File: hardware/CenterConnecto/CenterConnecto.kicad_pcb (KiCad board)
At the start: 2 copper layers, 21.5 x 12 mm, 4 parts, among them J1 Conn_01x10, J2 Conn_01x10

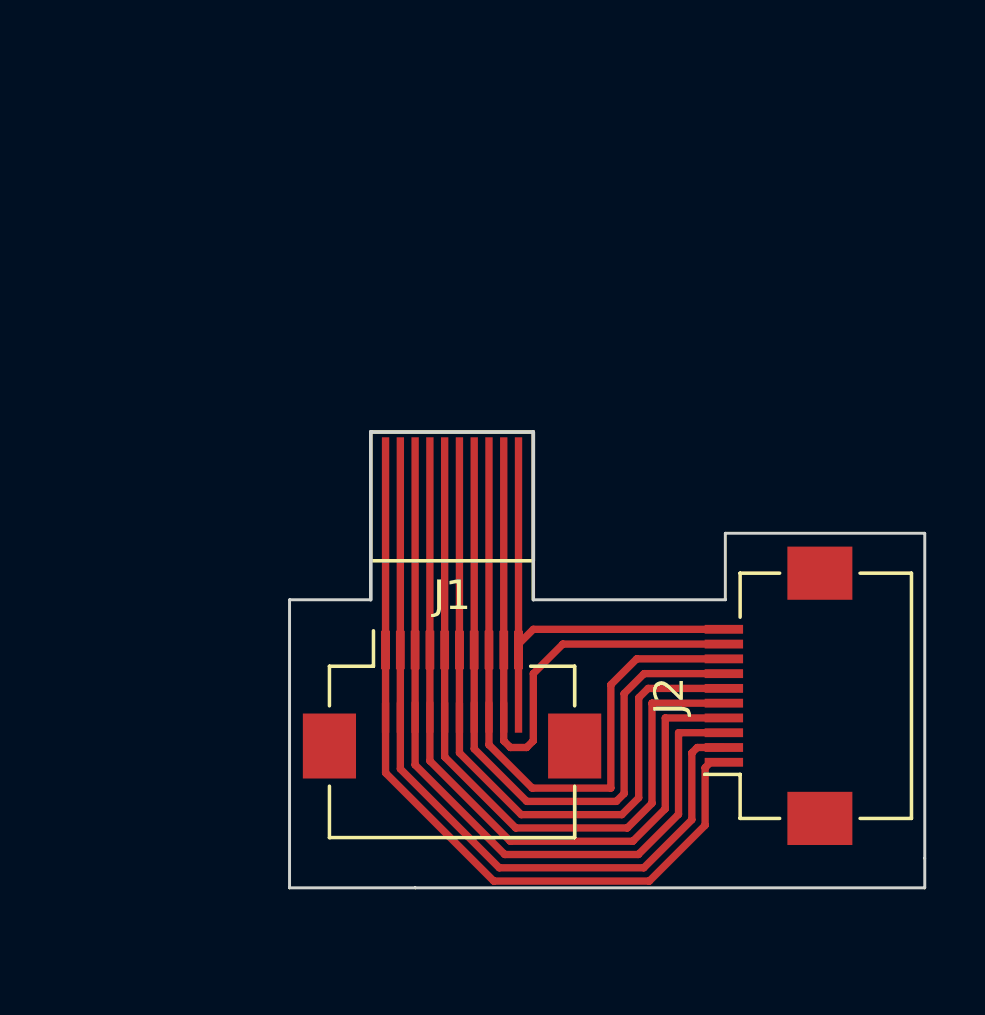
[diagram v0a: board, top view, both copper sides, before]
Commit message: Added initial left buttons fpc
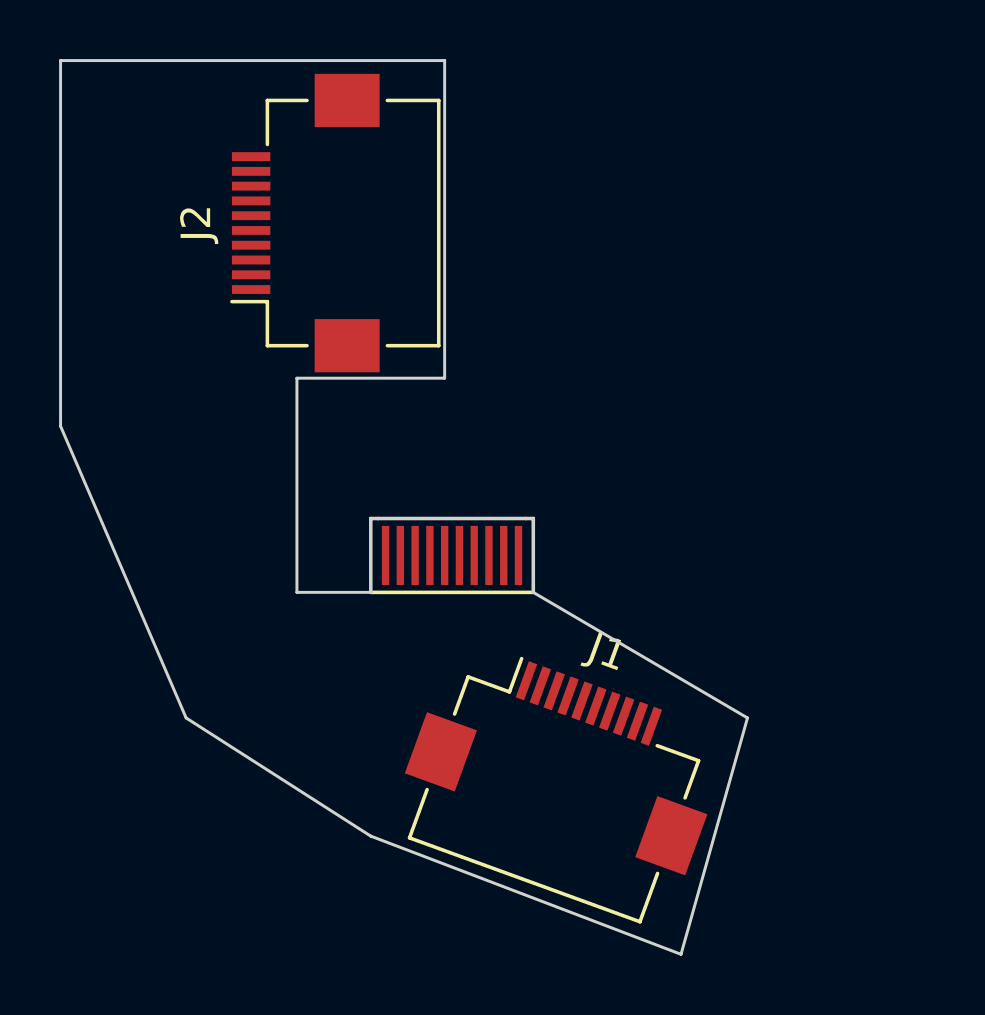
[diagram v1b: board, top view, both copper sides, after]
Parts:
- removed G***: LOGO, consolizer:QR
- C1: footprint consolizer:flex_long_10 -> consolizer:flex_short_10
- moved J2 22.6 mm to (148.6, 77.8)
- moved J1 4.35 mm to (157.5, 95.8), turned to -20 degrees
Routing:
- net /P1: track 18.1 -> 0.00 mm
- net /P2: track 17.6 -> 0.00 mm
- net /P3: track 16.8 -> 0.00 mm
- net /P4: track 16.3 -> 0.00 mm
- net /P5: track 15.7 -> 0.00 mm
- net /P6: track 15.0 -> 0.00 mm
- net /P7: track 14.2 -> 0.00 mm
- net /P8: track 13.5 -> 0.00 mm
- net /P9: track 11.3 -> 0.00 mm
- net /P10: track 7.06 -> 0.00 mm
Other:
- board size 21.5 x 12 mm -> 23.2 x 30.2 mm
